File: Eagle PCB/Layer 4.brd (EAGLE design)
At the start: 108.5 x 108.5 mm, 49 parts, among them X1 SM06B-SRSS-TB, Y1 8MHz

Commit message: Final
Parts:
- moved 3RD_LAYER 66.2 mm to (4.82, -33.3), turned to 180 degrees
- moved 3V3_PWR 61.1 mm to (-4.55, -35.8), turned to 90 degrees
- moved R4 9.22 mm to (-14.8, 32.3), turned to 180 degrees
- moved 1R4 3.85 mm to (0.01, -25.0), turned to 90 degrees
- moved TOF3 1.77 mm to (-17.7, -11.5)
- moved TOF4 0.82 mm to (20.2, -11.5)
- moved TOF2 0.37 mm to (22.9, 23.1)
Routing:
- net TX2: track 16.6 -> 54.8 mm, vias 1 -> 3
- net RX2: track 17.7 -> 52.2 mm, vias 1 -> 3
- net 3V3_SWITCH: track 205.8 -> 236.1 mm, vias 6 -> 8
- net 3.3V: track 33.4 -> 12.8 mm, vias 1 -> 0
- net BOOT0: track 35.0 -> 28.4 mm
- net L4R: track 39.2 -> 34.2 mm
- net GND: track 122.0 -> 125.4 mm
- net SHUT3: track 70.3 -> 71.4 mm
- net SCL1: track 159.8 -> 160.7 mm
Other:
- outline, holes or cut-outs redrawn

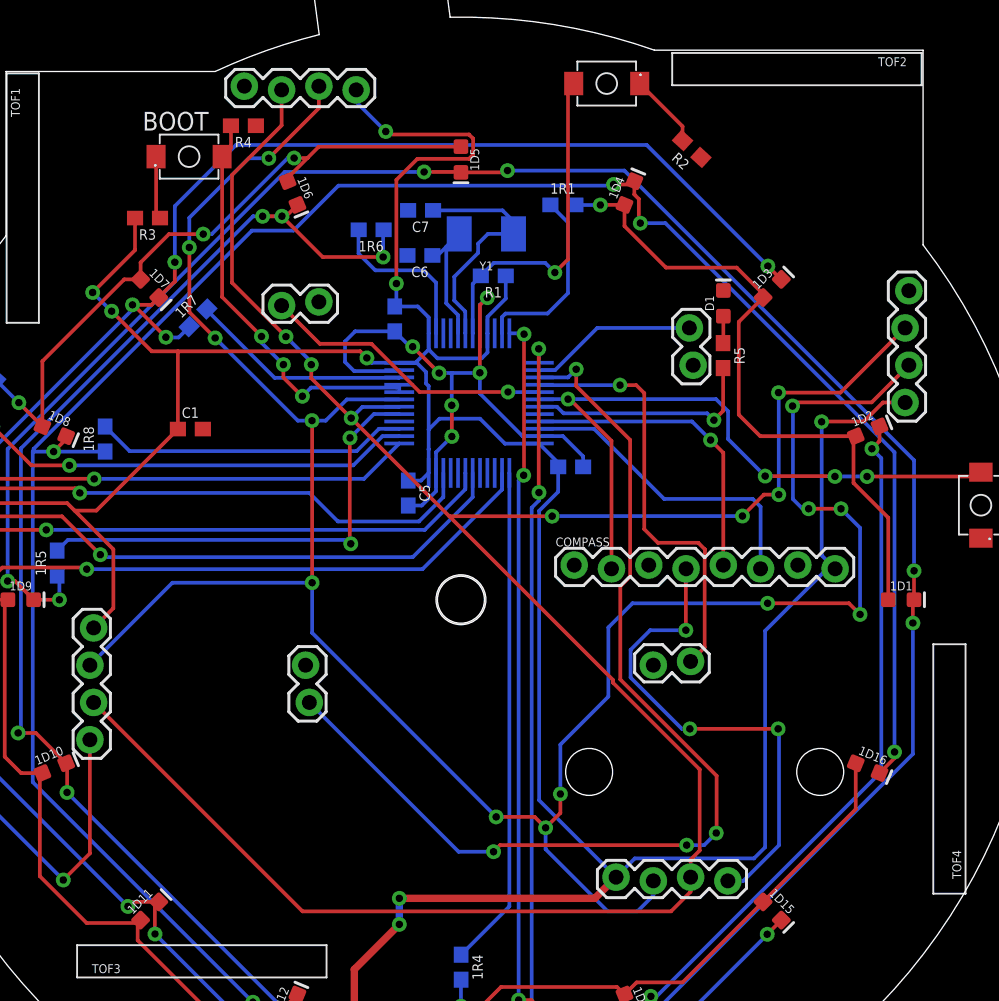
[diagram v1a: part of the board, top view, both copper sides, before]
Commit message: layer 1 esc fix
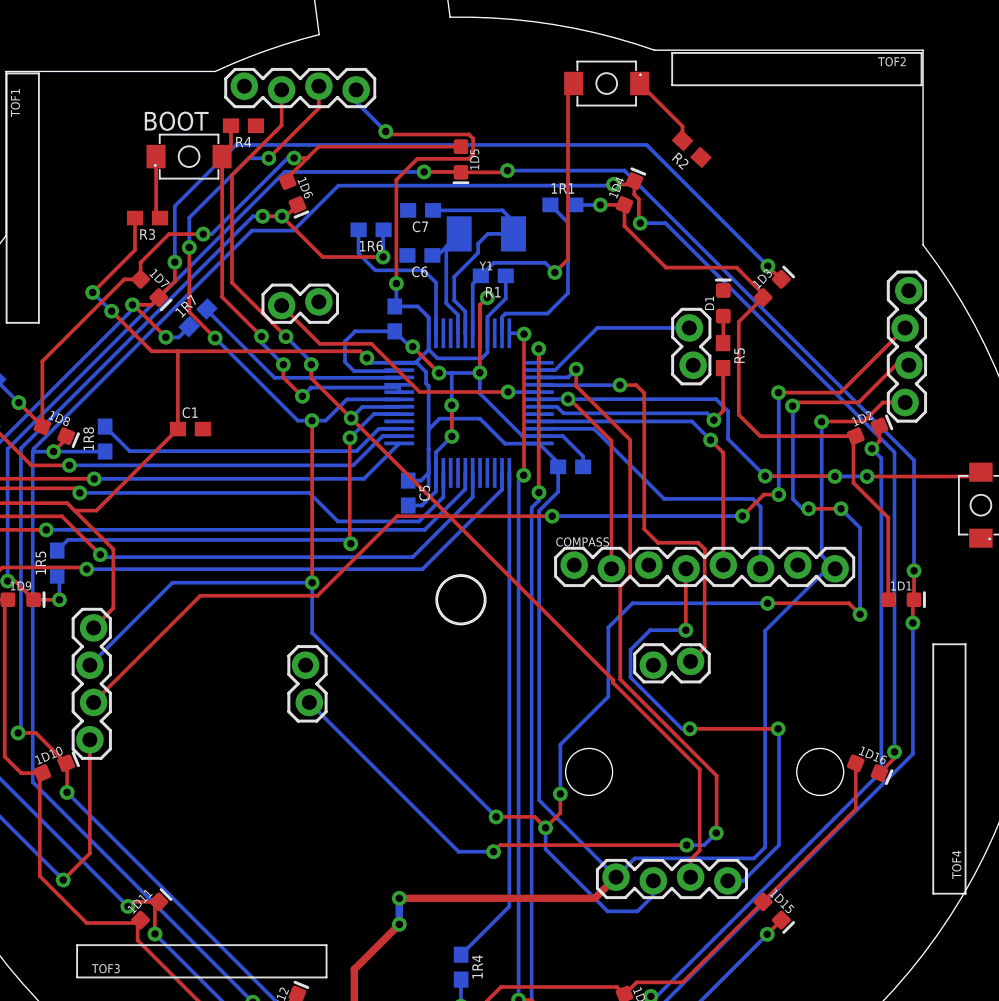
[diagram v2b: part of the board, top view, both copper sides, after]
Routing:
- net SCL1: track 160.7 -> 142.1 mm
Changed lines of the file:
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@@
 </layers>
 <board>
-<fusionsync huburn="a.YnVzaW5lc3M6Z21haWwxNDMxNzc3" projecturn="a.YnVzaW5lc3M6Z21haWwxNDMxNzc3I0QyMDIxMDEwODM2OTU2MDYzMQ" f3durn="urn:adsk.wipprod:dm.lineage:VfCCbaBsTTm4Gg6EPxi-vA" pcbguid="" lastpulledtime="" lastsyncedchangeguid="" latestrevisionid="867ffa56-129e-4ce6-882f-6d524e8d2100" lastsyncedrevisionid="867ffa56-129e-4ce6-882f-6d524e8d2100" lastboardhashguid="58c1dd92-876e-00cd-da6c-04a12a067a0c" lastpushedtime="2021-02-28T09:39:44Z" linktopcb3d="true"/>
+<fusionsync huburn="a.YnVzaW5lc3M6Z21haWwxNDMxNzc3" projecturn="a.YnVzaW5lc3M6Z21haWwxNDMxNzc3I0QyMDIxMDEwODM2OTU2MDYzMQ" f3durn="urn:adsk.wipprod:dm.lineage:VfCCbaBsTTm4Gg6EPxi-vA" pcbguid="" lastpulledtime="" lastsyncedchangeguid="" latestrevisionid="867ffa56-129e-4ce6-882f-6d524e8d2100" lastsyncedrevisionid="867ffa56-129e-4ce6-882f-6d524e8d2100" lastboardhashguid="58c1dd92-876e-00cd-da6c-04a12a067a0c" lastpushedtime="2021-02-28T09:39:44Z" linktopcb3d="false"/>
 <plain>
 <circle x="0" y="0" radius="1.6" width="0.001" layer="20"/>
@@
 <signal name="SDA2">
 <contactref element="STM32" pad="22"/>
-<contactref element="COMPASS" pad="6"/>
 <wire x1="19.88505" y1="6.869409375" x2="13.849009375" y2="6.869409375" width="0.254" layer="16"/>
 <wire x1="19.88505" y1="6.869409375" x2="20.41933125" y2="6.335128125" width="0.254" layer="16"/>
-<wire x1="20.41933125" y1="6.335128125" x2="20.41933125" y2="2.107159375" width="0.254" layer="16"/>
 <wire x1="5.308590625" y1="11.649090625" x2="9.069328125" y2="11.649090625" width="0.254" layer="16"/>
 <wire x1="9.069328125" y1="11.649090625" x2="13.849009375" y2="6.869409375" width="0.254" layer="16"/>
+<contactref element="COMPASS" pad="6"/>
+<wire x1="20.41933125" y1="6.335128125" x2="20.41933125" y2="2.107159375" width="0.254" layer="16"/>
 </signal>
 <signal name="SCL2">
 <contactref element="STM32" pad="21"/>
-<contactref element="COMPASS" pad="5"/>
 <wire x1="5.308590625" y1="12.149090625" x2="15.745459375" y2="12.149090625" width="0.254" layer="16"/>
 <wire x1="15.745459375" y1="12.149090625" x2="17.013996875" y2="10.880553125" width="0.254" layer="16"/>
 <via x="17.013996875" y="10.880553125" extent="1-16" drill="0.508"/>
 <wire x1="17.013996875" y1="10.880553125" x2="17.87933125" y2="10.01521875" width="0.254" layer="1"/>
+<contactref element="COMPASS" pad="5"/>
 <wire x1="17.87933125" y1="10.01521875" x2="17.87933125" y2="2.361159375" width="0.254" layer="1"/>
 </signal>
 <signal name="SDA1">
 <contactref element="STM32" pad="43"/>
-<contactref element="TOF1" pad="SDA"/>
-<contactref element="TOF2" pad="SDA"/>
-<contactref element="TOF3" pad="SDA"/>
-<contactref element="TOF4" pad="SDA"/>
 <wire x1="12.03185" y1="-21.235540625" x2="9.999965625" y2="-21.235540625" width="0.254" layer="16"/>
-<wire x1="30.52343125" y1="15.981340625" x2="27.991309375" y2="13.44921875" width="0.254" layer="1"/>
-<wire x1="27.991309375" y1="13.44921875" x2="22.84921875" y2="13.44921875" width="0.254" layer="1"/>
+<wire x1="27.111309375" y1="13.44921875" x2="22.84921875" y2="13.44921875" width="0.254" layer="1"/>
 <wire x1="22.84921875" y1="13.44921875" x2="22.6" y2="13.2" width="0.254" layer="1"/>
 <via x="22.6" y="13.2" extent="1-16" drill="0.508"/>
@@
 <via x="-13.096471875" y="30.0842" extent="1-16" drill="0.508"/>
 <wire x1="-13.096471875" y1="30.0842" x2="-9.68218125" y2="33.498490625" width="0.254" layer="1"/>
-<wire x1="-9.68218125" y1="33.498490625" x2="-9.68218125" y2="34.99828125" width="0.254" layer="1"/>
 <via x="6.775446875" y="-13.239903125" extent="1-16" drill="0.508"/>
 <wire x1="10.047" y1="-6.6005625" x2="10.047" y2="-1.885775" width="0.254" layer="16"/>
@@
 <wire x1="5.767953125" y1="-17.003528125" x2="5.767953125" y2="-15.54395" width="0.254" layer="16"/>
 <via x="5.767953125" y="-15.54395" extent="1-16" drill="0.508"/>
-<wire x1="-25.2868" y1="-4.46251875" x2="-19.665853125" y2="1.158428125" width="0.254" layer="16"/>
-<wire x1="-19.665853125" y1="1.158428125" x2="-10.1414875" y2="1.158428125" width="0.254" layer="16"/>
+<wire x1="-10.1414875" y1="1.158428125" x2="-19.665853125" y2="1.158428125" width="0.254" layer="16"/>
 <wire x1="22.625259375" y1="6.856203125" x2="23.2814625" y2="6.2" width="0.254" layer="16"/>
 <wire x1="23.2814625" y1="6.2" x2="23.69585" y2="6.2" width="0.254" layer="16"/>
@@
 <wire x1="26.443090625" y1="-0.243090625" x2="27.2" y2="-1" width="0.254" layer="1"/>
 <via x="27.2" y="-1" extent="1-16" drill="0.508"/>
-<wire x1="13.11001875" y1="-19.16033125" x2="13.11001875" y2="-20.157371875" width="0.254" layer="16"/>
-<wire x1="13.11001875" y1="-20.157371875" x2="12.03185" y2="-21.235540625" width="0.254" layer="16"/>
+<wire x1="12.03185" y1="-21.235540625" x2="13.11001875" y2="-20.157371875" width="0.254" layer="16"/>
+<contactref element="TOF1" pad="SDA"/>
+<contactref element="TOF2" pad="SDA"/>
+<contactref element="TOF3" pad="SDA"/>
+<contactref element="TOF4" pad="SDA"/>
+<wire x1="-19.665853125" y1="1.158428125" x2="-25.2868" y2="-4.46251875" width="0.254" layer="16"/>
+<wire x1="13.11001875" y1="-20.157371875" x2="13.11001875" y2="-19.16033125" width="0.254" layer="16"/>
+<wire x1="-9.68218125" y1="33.498490625" x2="-9.68218125" y2="34.99828125" width="0.254" layer="1"/>
+<wire x1="29.64343125" y1="15.981340625" x2="30.52343125" y2="15.981340625" width="0.254" layer="1"/>
+<wire x1="29.64343125" y1="15.981340625" x2="27.111309375" y2="13.44921875" width="0.254" layer="1"/>
 </signal>
 <signal name="SCL1">
 <contactref element="STM32" pad="42"/>
-<contactref element="TOF1" pad="SCL"/>
-<contactref element="TOF2" pad="SCL"/>
-<contactref element="TOF3" pad="SCL"/>
-<contactref element="TOF4" pad="SCL"/>
 <via x="-7.4809" y="12.376925" extent="1-16" drill="0.508"/>
 <wire x1="-4.207409375" y1="13.149090625" x2="-4.219996875" y2="13.136503125" width="0.254" layer="16"/>
 <wire x1="-4.219996875" y1="13.136503125" x2="-6.721321875" y2="13.136503125" width="0.254" layer="16"/>
 <wire x1="-7.4809" y1="12.376925" x2="-6.721321875" y2="13.136503125" width="0.254" layer="16"/>
-<wire x1="30.26943125" y1="18.521340625" x2="25.860978125" y2="14.1128875" width="0.254" layer="1"/>
-<wire x1="25.860978125" y1="14.1128875" x2="21.642284375" y2="14.1128875" width="0.254" layer="1"/>
+<wire x1="21.642284375" y1="14.1128875" x2="25.860978125" y2="14.1128875" width="0.254" layer="1"/>
 <via x="21.642284375" y="14.1128875" extent="1-16" drill="0.508"/>
 <wire x1="21.642284375" y1="14.1128875" x2="21.659359375" y2="14.0958125" width="0.254" layer="16"/>
 <wire x1="21.659359375" y1="14.0958125" x2="21.659359375" y2="7.162975" width="0.254" layer="16"/>
 <wire x1="19.17375625" y1="5.6907" x2="19.18305625" y2="5.7" width="0.254" layer="16"/>
-<wire x1="-10.79711875" y1="-21.2382" x2="14.315190625" y2="-21.2382" width="0.254" layer="1"/>
-<wire x1="-25.0328" y1="-7.00251875" x2="-10.79711875" y2="-21.2382" width="0.254" layer="1"/>
-<wire x1="-12.22218125" y1="32.324440625" x2="-15.6" y2="28.946621875" width="0.254" layer="1"/>
-<wire x1="-12.22218125" y1="34.74428125" x2="-12.22218125" y2="32.324440625" width="0.254" layer="1"/>
+<wire x1="-15.6" y1="28.946621875" x2="-12.22218125" y2="32.324440625" width="0.254" layer="1"/>
 <wire x1="-15.6" y1="28.946621875" x2="-15.6" y2="21.602328125" width="0.254" layer="1"/>
 <wire x1="-15.6" y1="21.602328125" x2="-11.925259375" y2="17.9275875" width="0.254" layer="1"/>
@@
 <wire x1="20.64603125" y1="7.162975" x2="21.659359375" y2="7.162975" width="0.254" layer="1"/>
 <via x="21.659359375" y="7.162975" extent="1-16" drill="0.508"/>
-<wire x1="14.315190625" y1="-21.2382" x2="15.65001875" y2="-19.903371875" width="0.254" layer="1"/>
-<wire x1="15.65001875" y1="-19.903371875" x2="15.65001875" y2="-18.90633125" width="0.254" layer="1"/>
-<wire x1="15.65001875" y1="-18.90633125" x2="15.65001875" y2="-17.714975" width="0.254" layer="1"/>
-<wire x1="15.65001875" y1="-17.714975" x2="16.27064375" y2="-17.09435" width="0.254" layer="1"/>
+<wire x1="16.27064375" y1="-17.09435" x2="15.65001875" y2="-17.714975" width="0.254" layer="1"/>
 <wire x1="-7.4809" y1="12.376925" x2="-0.794675" y2="5.6907" width="0.254" layer="1"/>
 <wire x1="16.27064375" y1="-11.5636625" x2="10.352" y2="-5.64501875" width="0.254" layer="1"/>
@@
 <via x="6.217425" y="5.6907" extent="1-16" drill="0.508"/>
 <wire x1="6.217425" y1="5.6907" x2="-0.794675" y2="5.6907" width="0.254" layer="1"/>
+<contactref element="TOF1" pad="SCL"/>
+<contactref element="TOF2" pad="SCL"/>
+<contactref element="TOF3" pad="SCL"/>
+<contactref element="TOF4" pad="SCL"/>
+<wire x1="-25.0328" y1="-7.00251875" x2="-17.76085" y2="0.26943125" width="0.254" layer="1"/>
+<wire x1="-17.76085" y1="0.26943125" x2="-9.77325" y2="0.26943125" width="0.254" layer="1"/>
+<wire x1="-4.35198125" y1="5.6907" x2="-0.794675" y2="5.6907" width="0.254" layer="1"/>
+<wire x1="-9.77325" y1="0.26943125" x2="-4.35198125" y2="5.6907" width="0.254" layer="1"/>
+<wire x1="15.65001875" y1="-17.714975" x2="15.65001875" y2="-18.90633125" width="0.254" layer="1"/>
+<wire x1="-12.22218125" y1="32.324440625" x2="-12.22218125" y2="34.74428125" width="0.254" layer="1"/>
+<wire x1="25.860978125" y1="14.1128875" x2="30.26943125" y2="18.521340625" width="0.254" layer="1"/>
 </signal>
 <signal name="SHUT2">
